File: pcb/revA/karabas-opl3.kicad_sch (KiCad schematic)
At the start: 63 parts, among them J1 Conn_02x05_Odd_Even, J2 Conn_02x30_Row_Letter_First, J3 PJ307, J4 Conn_01x04, J5 5V_PRG, SW1 SW_DIP_x05, U1 YMF262-M, U2 74AHCT1G125DB, U3 EPM3128ATC100, U4 UDA1334ATS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

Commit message: Added debug leds
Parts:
- added D1: DBG1, LED_SMD:LED_0805_2012Metric_Pad1.15x1.40mm_HandSolder, symbol Device:LED
- added D2: DBG2, LED_SMD:LED_0805_2012Metric_Pad1.15x1.40mm_HandSolder, symbol Device:LED
- added R20, R21: 1k, Resistor_SMD:R_0805_2012Metric_Pad1.20x1.40mm_HandSolder, symbol Device:R
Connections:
- net +3V3: now also R20.1, R21.1
- net GND: no longer U4.11 (SFOR0)
- net LED2: now reaches U3.69 (I/O)
- net LED2: now also D2.1 (K)
- net LED1: now reaches U3.71 (I/O)
- net LED1: now also D1.1 (K)
- net DAC_STD: now reaches U3.85 (I/O)
- net DAC_STD: now also U4.11 (SFOR0)
- new net: D2.2 (A), R21.2
- new net: D1.2 (A), R20.2
- no-connect marks 54 -> 51
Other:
- moved on the sheet: JP1

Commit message: Added universal footprint for 3225+5070 osc
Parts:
- X1: footprint my:Oscillator_SMD_7050_7.0x5.0mm -> footprints:Oscillator_SMD_7050_7.0x5.0mm_mixed_3225
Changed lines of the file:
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@@
 			)
 		)
-		(property "Footprint" "my:Oscillator_SMD_7050_7.0x5.0mm"
+		(property "Footprint" "footprints:Oscillator_SMD_7050_7.0x5.0mm_mixed_3225"
 			(at 207.01 158.75 0)
 			(effects

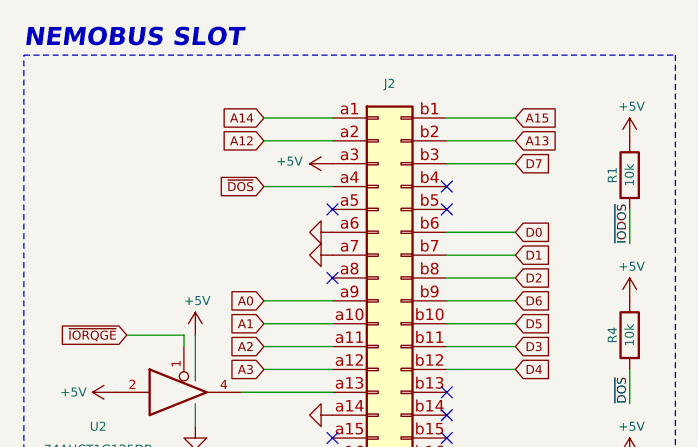
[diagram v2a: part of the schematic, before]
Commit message: Updated 5V lane - removed loop
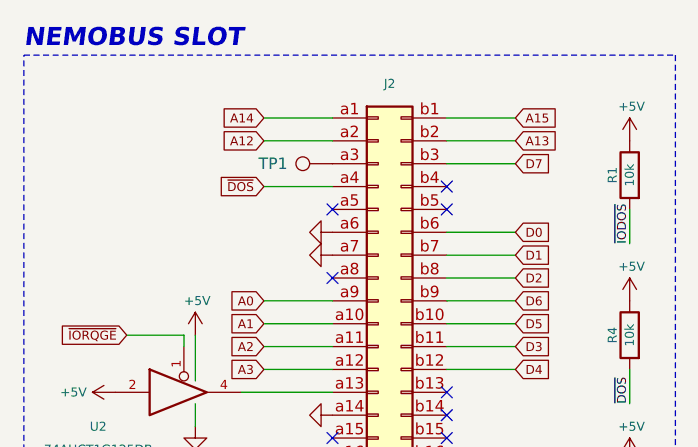
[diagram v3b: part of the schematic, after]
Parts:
- added TP1: +5V, TestPoint:TestPoint_Keystone_5015_Micro_Mini, symbol Connector:TestPoint
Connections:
- net +5V: no longer J2.a3 (Pin_a3)
- new net: J2.a3 (Pin_a3), TP1.1
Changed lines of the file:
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@@
-	)
-	(symbol
-		(lib_id "power:+5V")
-		(at 50.8 30.48 90)
-		(unit 1)
-		(exclude_from_sim no)
-		(in_bom yes)
-		(on_board yes)
-		(dnp no)
-		(property "Reference" "#PWR04"
-			(at 54.61 30.48 0)
-			(effects
-				(font
-					(size 1 1)
-				)
-				(hide yes)
-			)
-		)
-		(property "Value" "+5V"
-			(at 47.498 30.226 90)
-			(effects
-				(font
-					(size 1 1)
-				)
-				(justify left)
-			)
-		)
-		(property "Footprint" ""
-			(at 50.8 30.48 0)
-			(effects
-				(font
-					(size 1.27 1.27)
-				)
-				(hide yes)
-			)
-		)
-		(property "Datasheet" ""
-			(at 50.8 30.48 0)
-			(effects
-				(font
-					(size 1.27 1.27)
-				)
-				(hide yes)
-			)
-		)
-		(property "Description" "Power symbol creates a global label with name \"+5V\""
-			(at 50.8 30.48 0)
-			(effects
-				(font
-					(size 1.27 1.27)
-				)
-				(hide yes)
-			)
-		)
-		(pin "1"
-		)
-		(instances
-			(project "karabas-opl3"
-				(path "/eff1afb7-47ba-46af-a815-4a07fb8d674b"
-					(reference "#PWR04")
-					(unit 1)
-				)
-			)
-		)
 	)
 	(symbol
@@
 					(unit 1)
 				)
+			)
+		)
+	)
+	(symbol
+		(lib_id "Connector:TestPoint")
+		(at 50.8 30.48 90)
+		(unit 1)
+		(exclude_from_sim no)
+		(in_bom yes)
+		(on_board yes)
+		(dnp no)
+		(property "Reference" "TP1"
+			(at 44.196 30.48 90)
+			(effects
+				(font
+					(size 1.27 1.27)
+				)
+			)
+		)
+		(property "Value" "+5V"
+			(at 47.498 27.94 90)
+			(effects
+				(font
+					(size 1.27 1.27)
+				)
+				(hide yes)
+			)
+		)
+		(property "Footprint" "TestPoint:TestPoint_Keystone_5015_Micro_Mini"
+			(at 50.8 25.4 0)
+			(effects
+				(font
+					(size 1.27 1.27)
+				)
+				(hide yes)
+			)
+		)
+		(property "Datasheet" "~"
+			(at 50.8 25.4 0)
+			(effects
+				(font
+					(size 1.27 1.27)
+				)
+				(hide yes)
+			)
+		)
+		(property "Description" "test point"
+			(at 50.8 30.48 0)
+			(effects
+				(font
+					(size 1.27 1.27)
+				)
+				(hide yes)
+			)
+		)
+		(pin "1"
+		)
+		(instances
+			(project ""
+				(path "/eff1afb7-47ba-46af-a815-4a07fb8d674b"
+					(reference "TP1")
+					(unit 1)
+				)

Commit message: Small footprint fixes
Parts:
- U1: footprint Package_SO:SOIC-24W_7.5x15.4mm_P1.27mm -> footprints:ymf-262-m
- U4: footprint Package_SO:SSOP-16_4.4x5.2mm_P0.65mm -> footprints:SSOP-16_4.4x5.2mm_P0.65mm-extended
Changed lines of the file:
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@@
 			)
 		)
-		(property "Footprint" "Package_SO:SSOP-16_4.4x5.2mm_P0.65mm"
+		(property "Footprint" "footprints:SSOP-16_4.4x5.2mm_P0.65mm-extended"
 			(at 208.28 104.14 0)
 			(effects
@@
 			)
 		)
-		(property "Footprint" "Package_SO:SOIC-24W_7.5x15.4mm_P1.27mm"
+		(property "Footprint" "footprints:ymf-262-m"
 			(at 194.31 29.21 0)
 			(effects
